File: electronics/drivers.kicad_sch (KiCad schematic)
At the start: 93 parts, among them J10 Conn_01x05_Pin, J11 Conn_01x01_Pin, J12 Conn_01x01_Pin, J13 Conn_01x02_Pin, J14 Conn_01x02_Pin, J15 VMOT, J16 IOLV / VIO, J17 GND, J18 EXPANSION_HDR, J2 CONT_CFG_DBG, J21 BYPASS_MOTOR_ENABLE, J3 Conn_01x04_Pin, J4 CONT_CFG_DBG, J5 Conn_01x04_Pin, J6 Conn_01x04_Pin, J7 Conn_01x04_Pin, J8 CONT_CFG_DBG, J9 CONT_CFG_DBG, Q3 Q_PMOS, U10 LM1117DT-3.3, U11 74LVC125, U12 ISO7762DBQ, U3 BTT TMC5160 Pro, U4 BTT TMC5160 Pro, U5 BTT TMC5160 Pro, U6 BTT TMC5160 Pro, U8 SFH617A-1, U9 SFH617A-1

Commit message: saving before i nuke this shit
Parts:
- removed C10, C12, C16, C9: 4.7uF, Capacitor_SMD:C_1210_3225Metric_Pad1.33x2.70mm_HandSolder, symbol Device:C_Polarized
- removed C11, C13, C15, C31: 100uF, Capacitor_THT:CP_Radial_D8.0mm_P5.00mm, symbol Device:C_Polarized
- removed C2: 100uF, Capacitor_SMD:C_0805_2012Metric_Pad1.18x1.45mm_HandSolder, symbol Device:C
- removed C23, C4: 100nF, Capacitor_SMD:C_0805_2012Metric_Pad1.18x1.45mm_HandSolder, symbol Device:C
- removed C24, C8: 100nF, Capacitor_SMD:C_0805_2012Metric_Pad1.18x1.45mm_HandSolder, symbol Device:C_Polarized
- removed C25: 100uF, Capacitor_THT:CP_Radial_D6.3mm_P2.50mm, symbol Device:C_Polarized
- removed C6: 4.7uF_100v, Capacitor_SMD:C_1210_3225Metric_Pad1.33x2.70mm_HandSolder, symbol Device:C_Polarized
- removed C7: 100uF_100v, Capacitor_THT:CP_Radial_D8.0mm_P5.00mm, symbol Device:C_Polarized
- removed D2, D3, D4, D5: 60V, symbol Device:D_TVS
- removed F1, F2, F3, F4, F5: Fuse, symbol Device:Fuse
- removed J10: Conn_01x05_Pin, symbol Connector:Conn_01x05_Pin
- removed J11, J12: Conn_01x01_Pin, symbol Connector:Conn_01x01_Pin
- removed J13, J14: Conn_01x02_Pin, symbol Connector:Conn_01x02_Pin
- removed J18: EXPANSION_HDR, symbol Connector:Conn_01x07_Pin
- removed J2, J4, J8, J9: CONT_CFG_DBG, symbol Driver_Motor:CONN_MOTOR
- removed J3, J5, J6, J7: Conn_01x04_Pin, symbol Connector:Conn_01x04_Pin
- removed L1: L, symbol Device:L
- removed L2, L3, L4, L5: L_Ferrite, symbol Device:L_Ferrite
- removed Q3: Q_PMOS, symbol Device:Q_PMOS
- removed R10, R11, R12, R13, R14, R15, R16, R17, R22, R23, R25, R26, R27, R8, R9: 33R, symbol Device:R
- removed U3, U4, U5, U6: BTT TMC5160 Pro, symbol Driver_Motor:BTT-TMC5160-PRO-v1_0
- added C20: 100nF, Capacitor_SMD:C_0805_2012Metric_Pad1.18x1.45mm_HandSolder, symbol Device:C
- added D5, D9: D_Schottky, Diode_THT:D_DO-201AD_P3.81mm_Vertical_AnodeUp, symbol Device:D_Schottky
- added D8: 60V, Diode_THT:D_DO-41_SOD81_P2.54mm_Vertical_AnodeUp, symbol Device:D_TVS
- added J10: Conn_01x02_Pin, Connector_PinSocket_2.54mm:PinSocket_1x02_P2.54mm_Vertical, symbol Connector:Conn_01x02_Pin
- added J13: Conn_01x08_Pin, Connector_PinSocket_2.54mm:PinSocket_1x08_P2.54mm_Vertical, symbol Connector:Conn_01x08_Pin
- added Q2: PMOS_GDS, Package_TO_SOT_THT:TO-220-3_Vertical, symbol Transistor_FET:Q_PMOS_GDS
- added R46: 0, Jumper:SolderJumper-2_P1.3mm_Open_Pad1.0x1.5mm, symbol Device:R
- added R94: 100k, Resistor_SMD:R_0805_2012Metric_Pad1.20x1.40mm_HandSolder, symbol Device:R
- C17: renamed from C14; V (none) -> 100V
- C21: renamed from C3; V (none) -> 10V
- C22: renamed from C5; value 100n -> 100nF; V (none) -> 10V
- C23: renamed from C18; V (none) -> 50v
- C24: renamed from C1; footprint Capacitor_SMD:C_0805_2012Metric_Pad1.18x1.45mm_HandSolder -> Capacitor_THT:CP_Radial_D5.0mm_P2.50mm; V (none) -> 50V
- C25: renamed from C28; V (none) -> 10V
- C26: V (none) -> 10V
- D6: renamed from D1; value D_Zener -> Zener-12v; footprint (none) -> Diode_THT:D_DO-41_SOD81_P2.54mm_Vertical_AnodeUp
- D7: renamed from D8; footprint (none) -> Diode_THT:D_DO-41_SOD81_P2.54mm_Vertical_AnodeUp
- FB2: renamed from FB1; footprint (none) -> Inductor_SMD:L_1210_3225Metric_Pad1.42x2.65mm_HandSolder
- J12: renamed from J17; footprint (none) -> Connector_PinSocket_2.54mm:PinSocket_1x08_P2.54mm_Vertical
- J14: renamed from J16; footprint (none) -> Connector_PinSocket_2.54mm:PinSocket_1x08_P2.54mm_Vertical
- J8: renamed from J15; footprint (none) -> Connector_PinSocket_2.54mm:PinSocket_1x08_P2.54mm_Vertical
- J9: renamed from J21; value BYPASS_MOTOR_ENABLE -> BP_MOTOR_ENABLE; footprint (none) -> Connector_PinSocket_2.54mm:PinSocket_1x03_P2.54mm_Vertical
- R38: renamed from R4; footprint (none) -> Resistor_SMD:R_0805_2012Metric_Pad1.20x1.40mm_HandSolder
- R39: renamed from R6; footprint (none) -> Resistor_SMD:R_0805_2012Metric_Pad1.20x1.40mm_HandSolder
- R40: renamed from R37; value 1k -> 10k; footprint (none) -> Resistor_SMD:R_0805_2012Metric_Pad1.20x1.40mm_HandSolder
- R41: renamed from R51; footprint (none) -> Resistor_THT:R_Axial_DIN0204_L3.6mm_D1.6mm_P1.90mm_Vertical
- R42: renamed from R19; footprint (none) -> Resistor_SMD:R_0805_2012Metric_Pad1.20x1.40mm_HandSolder
- R43: renamed from R21; footprint (none) -> Resistor_SMD:R_0805_2012Metric_Pad1.20x1.40mm_HandSolder
- R44: renamed from R20; footprint (none) -> Resistor_SMD:R_0805_2012Metric_Pad1.20x1.40mm_HandSolder
- R45: renamed from R24; footprint (none) -> Resistor_SMD:R_0805_2012Metric_Pad1.20x1.40mm_HandSolder
- R47: renamed from R7; value 10k -> 1k; footprint (none) -> Resistor_THT:R_Axial_DIN0204_L3.6mm_D1.6mm_P1.90mm_Vertical
- R48: renamed from R50; footprint (none) -> Resistor_THT:R_Axial_DIN0204_L3.6mm_D1.6mm_P1.90mm_Vertical
- U11: renamed from U10; footprint Package_TO_SOT_SMD:TO-252-3_TabPin2 -> Package_TO_SOT_THT:TO-220-3_Vertical
- U9: renamed from U11; footprint (none) -> Package_DIP:DIP-14_W7.62mm
- renumbered U12 to U10, U8 to U12, U9 to U8
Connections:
- net GND: now also C21.2, C20.1, D8.2 (A2), J13.8 (Pin_8), R94.1; no longer C21.1
- net IOLV_IN: now also D9.2 (A); no longer C23.1, C24.1, U11.3 (VI)
- net MOTOR_PWR: now also D5.1 (K), Q2.3 (S)
- net V_IO_ISOLATED: now also C20.2
- net at D6.2 (A), R38.2, R39.1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: now also Q2.1 (G)
- net at U9.9: now also R44.1; no longer R44.2
- net DRV_VIO_ISO: now reaches C26.1
- net DRV_VIO_ISO: now also C21.1, C22.1, D7.2 (A2), FB2.2, J14.1 (Pin_1), J14.2 (Pin_2), J14.3 (Pin_3), J14.4 (Pin_4), R47.1, U10.16 (Vcc2), U9.14 (VCC), J13.4 (Pin_4)
- net at R45.1: now also U9.12; no longer U10.12 (OUTD)
- net at R45.2: now also U10.12 (OUTD); no longer U9.12
- net at U10.13 (OUTC): now also R44.2; no longer R44.1
- net at U10.10 (INF): now also J10.2 (Pin_2), R94.2
- net at U10.7 (OUTF): now also J10.1 (Pin_1)
- net DRIVER_ENABLE renamed DRV_ENABLE_ISO
- net DRV_ENABLE_ISO: now also J13.3 (Pin_3)
- net DRV_CLK renamed DRV_CLK_ISO
- net DRV_CLK_ISO: now also J13.7 (Pin_7)
- net DRV_DATA_CLK renamed DRV_SCK_ISO
- net DRV_SCK_ISO: now also J13.5 (Pin_5)
- net DRV_DATA_CS renamed DRV_CS_ISO
- net DRV_CS_ISO: now also J13.6 (Pin_6)
- net DRV_DATA_IN renamed DRV_MOSI_ISO
- net DRV_DATA_OUT renamed MCU_MISO_ISO
- net MCU_MISO_ISO: now also J13.1 (Pin_1), R46.2
- removed net V_io: C21.2, C22.1, D7.2 (A2), FB2.2, J14.1 (Pin_1), J14.2 (Pin_2), J14.3 (Pin_3), J14.4 (Pin_4), R47.1, U10.16 (Vcc2), U9.14 (VCC)
- net V_mot renamed VMOT
- net VMOT: now also D5.2 (A), D8.1 (A1), Q2.2 (D)
- new net: C23.1, C24.1, D9.1 (K), U11.3 (VI)
- new net DRV_MOSI_LAST: J13.2 (Pin_2), R46.1
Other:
- added sheet motor_driver (motor_driver.kicad_sch)
- added sheet motor_driver1 (motor_driver.kicad_sch)
- added sheet motor_driver2 (motor_driver.kicad_sch)
- added sheet motor_driver3 (motor_driver.kicad_sch)
- moved on the sheet: C17, C21, C23, C24, C25, D6, D7, FB2, J12, J14, J8, J9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

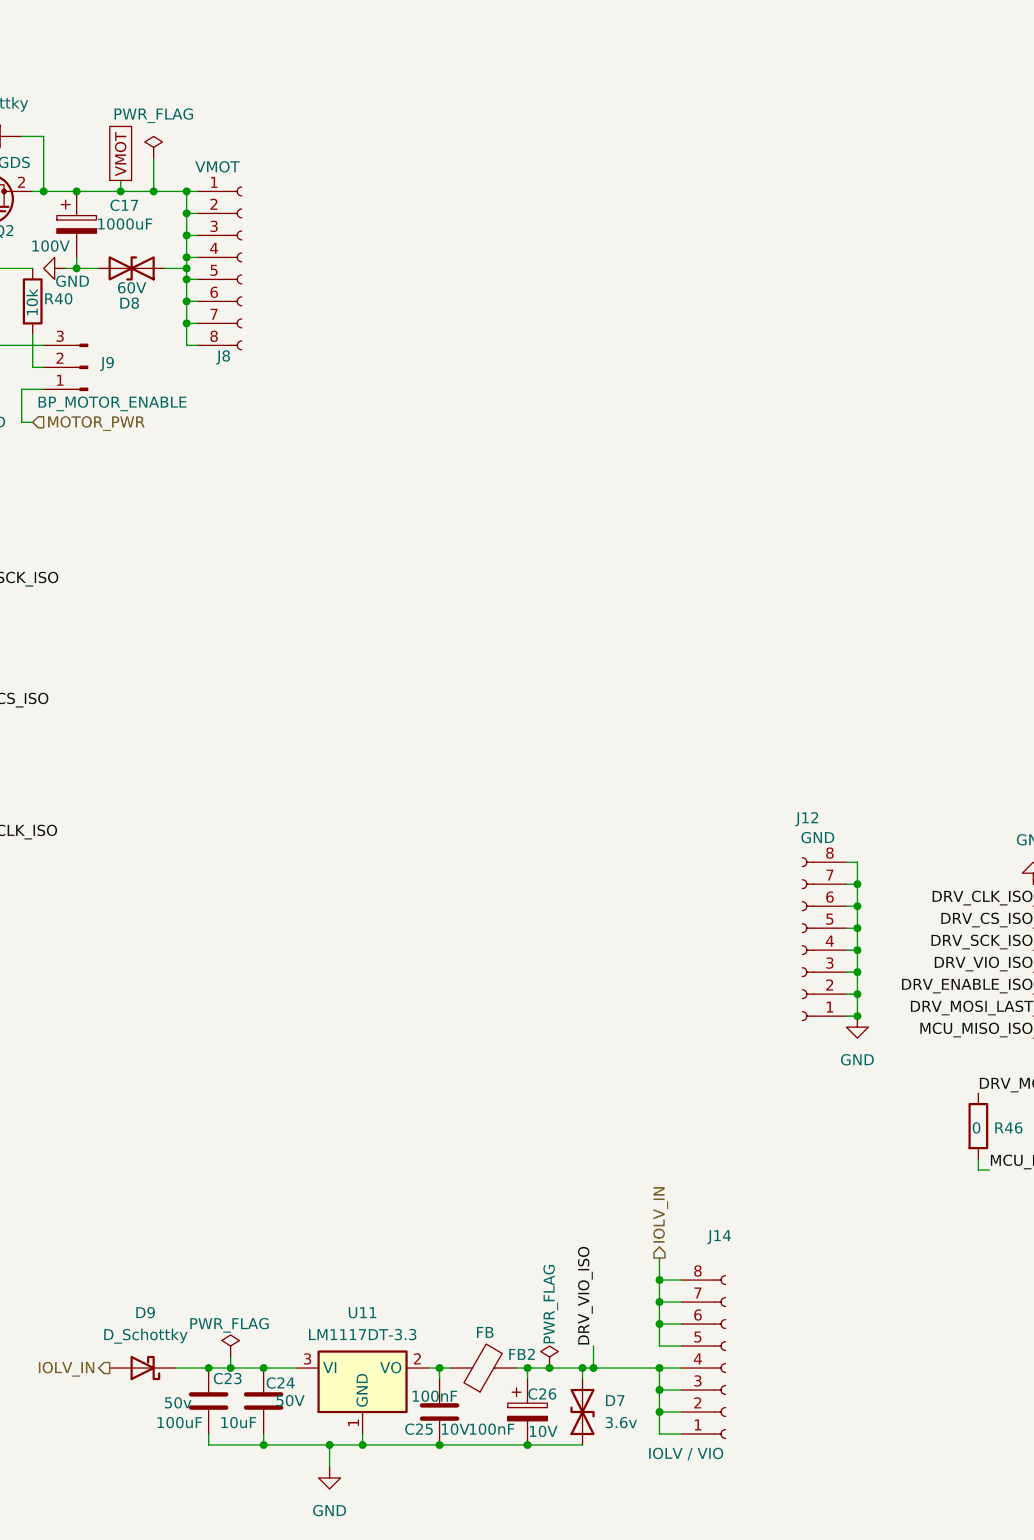
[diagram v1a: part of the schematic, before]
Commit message: Switching to a bigger PCB since cost seems negligible
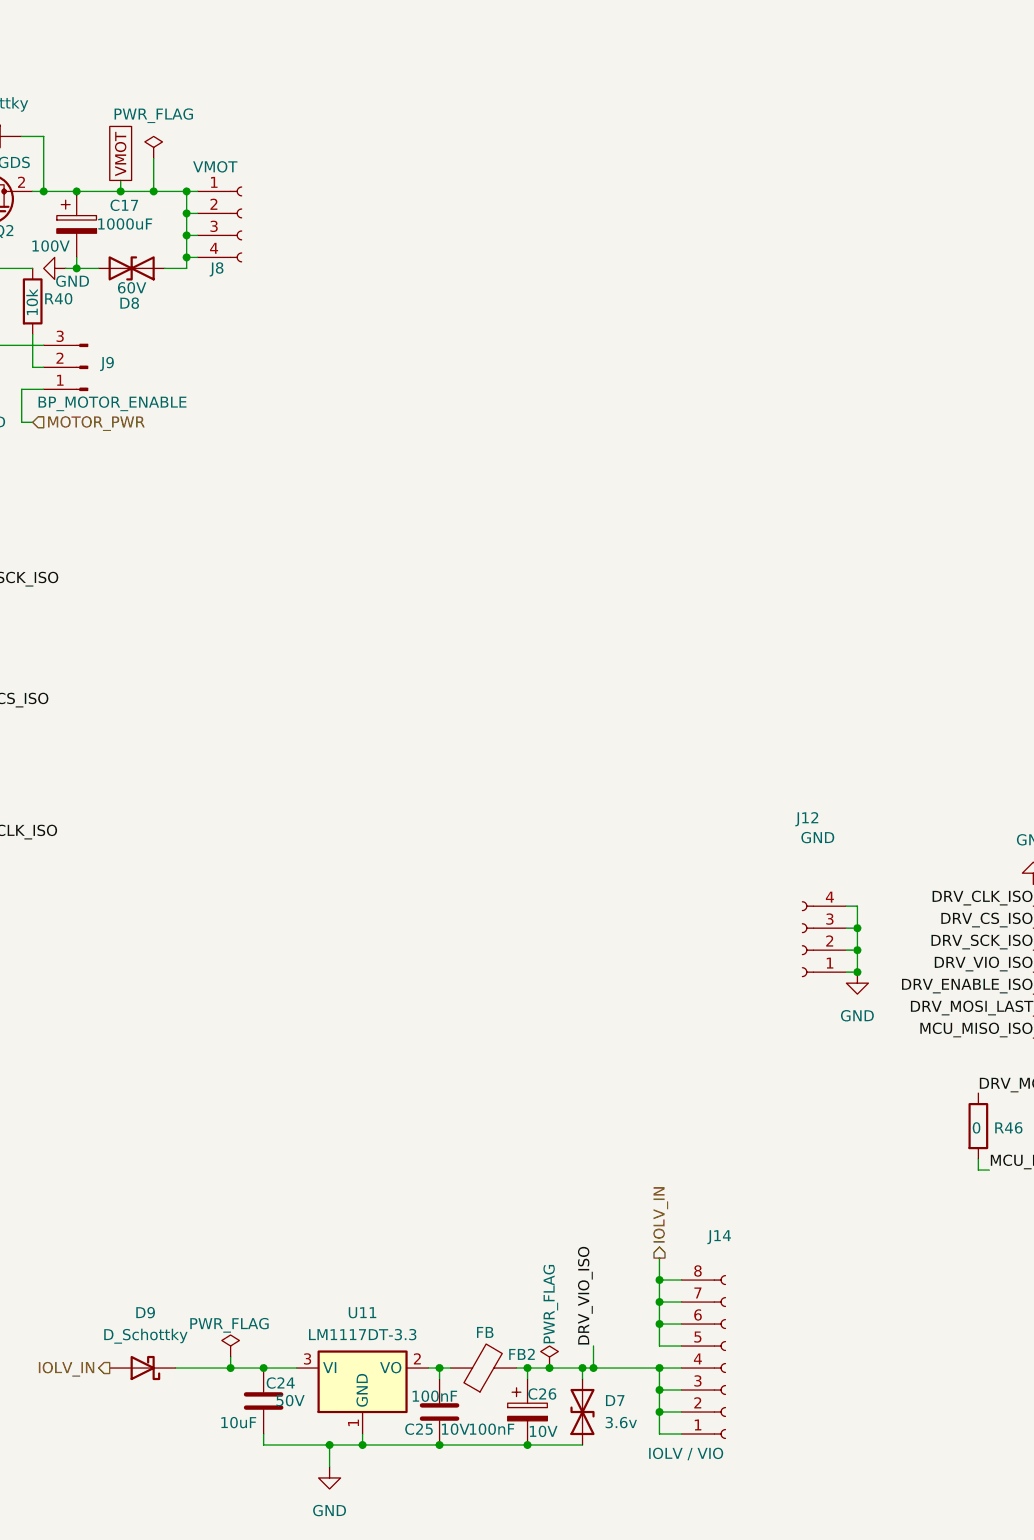
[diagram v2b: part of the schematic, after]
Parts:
- removed C23: 100uF, Capacitor_THT:CP_Radial_D8.0mm_P5.00mm, symbol Device:C
- J12, J8: footprint Connector_PinSocket_2.54mm:PinSocket_1x08_P2.54mm_Vertical -> Connector_PinSocket_2.54mm:PinSocket_1x04_P2.54mm_Vertical; symbol Connector:Conn_01x08_Socket -> Connector:Conn_01x04_Socket
- J13, J14: footprint Connector_PinSocket_2.54mm:PinSocket_1x08_P2.54mm_Vertical -> Connector_PinSocket_2.54mm:PinSocket_2x04_P2.54mm_Vertical
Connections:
- net GND: no longer J12.5 (Pin_5), J12.6 (Pin_6), J12.7 (Pin_7), J12.8 (Pin_8)
- net VMOT: no longer J8.5 (Pin_5), J8.6 (Pin_6), J8.7 (Pin_7), J8.8 (Pin_8)

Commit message: Updating electronics CAD post-production
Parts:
- added C11: 100uF, Capacitor_THT:CP_Radial_D6.3mm_P2.50mm, symbol Device:C_Polarized
- added R32, R34, R35: 0, Jumper:SolderJumper-2_P1.3mm_Open_Pad1.0x1.5mm, symbol Device:R
- D5, D9: footprint Diode_THT:D_DO-201AD_P3.81mm_Vertical_AnodeUp -> Diode_THT:D_DO-201AD_P5.08mm_Vertical_KathodeUp
- D8: footprint Diode_THT:D_DO-41_SOD81_P2.54mm_Vertical_AnodeUp -> Diode_THT:D_DO-201AD_P5.08mm_Vertical_KathodeUp
- R41, R47: footprint Resistor_THT:R_Axial_DIN0204_L3.6mm_D1.6mm_P1.90mm_Vertical -> Resistor_THT:R_Axial_DIN0204_L3.6mm_D1.6mm_P2.54mm_Vertical
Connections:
- net DRV_CLK_ISO: now also R32.1; no longer J13.7 (Pin_7)
- net DRV_CS_ISO: now also R34.1; no longer J13.6 (Pin_6)
- net DRV_SCK_ISO: now also R35.1; no longer J13.5 (Pin_5)
- net GND: now also C11.2
- net at C25.1, FB2.1, U11.2 (VO): now also C11.1
- new net: J13.5 (Pin_5), R35.2
- new net: J13.6 (Pin_6), R34.2
- new net: J13.7 (Pin_7), R32.2
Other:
- moved on the sheet: C24, C25, D9, J13, U11

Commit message: Some vibe coding to set up project structure. Almost all of the code will be rewritten to my standards
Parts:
- C11, C17, C24, D8, Q2, U11, U12, U8: msrcrt (none) -> Y
- C20, C21, C22, C25, C26, D7, FB2, J10, J9, R32, R34, R35, R38, R39, R40, R41, R42, R43, R44, R45, R46, R47, R48, R94, U10, U9: msrcrt (none) -> NA
- D5, D9, J12, J13, J14, J8: msrcrt (none) -> N
- D6: value Zener-12v -> Zen_12v; msrcrt (none) -> N
